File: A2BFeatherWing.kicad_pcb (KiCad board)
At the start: 2 copper layers, 50.8 x 22.9 mm, 5 parts, among them J1 Conn_01x04_Male, U1 FeatherWingTemplate, U2 AD2428W

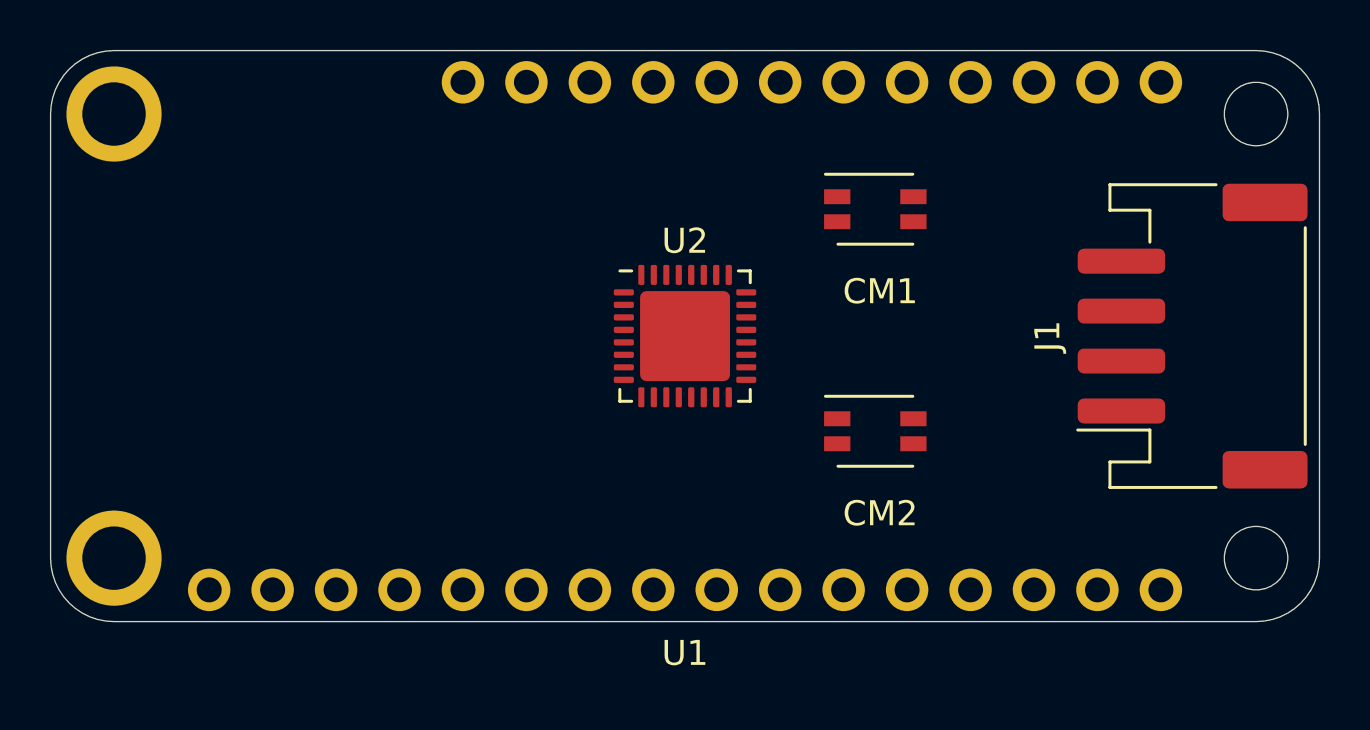
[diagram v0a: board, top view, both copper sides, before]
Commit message: added 3d model of JST PH and CM added eco layer for silkscreen
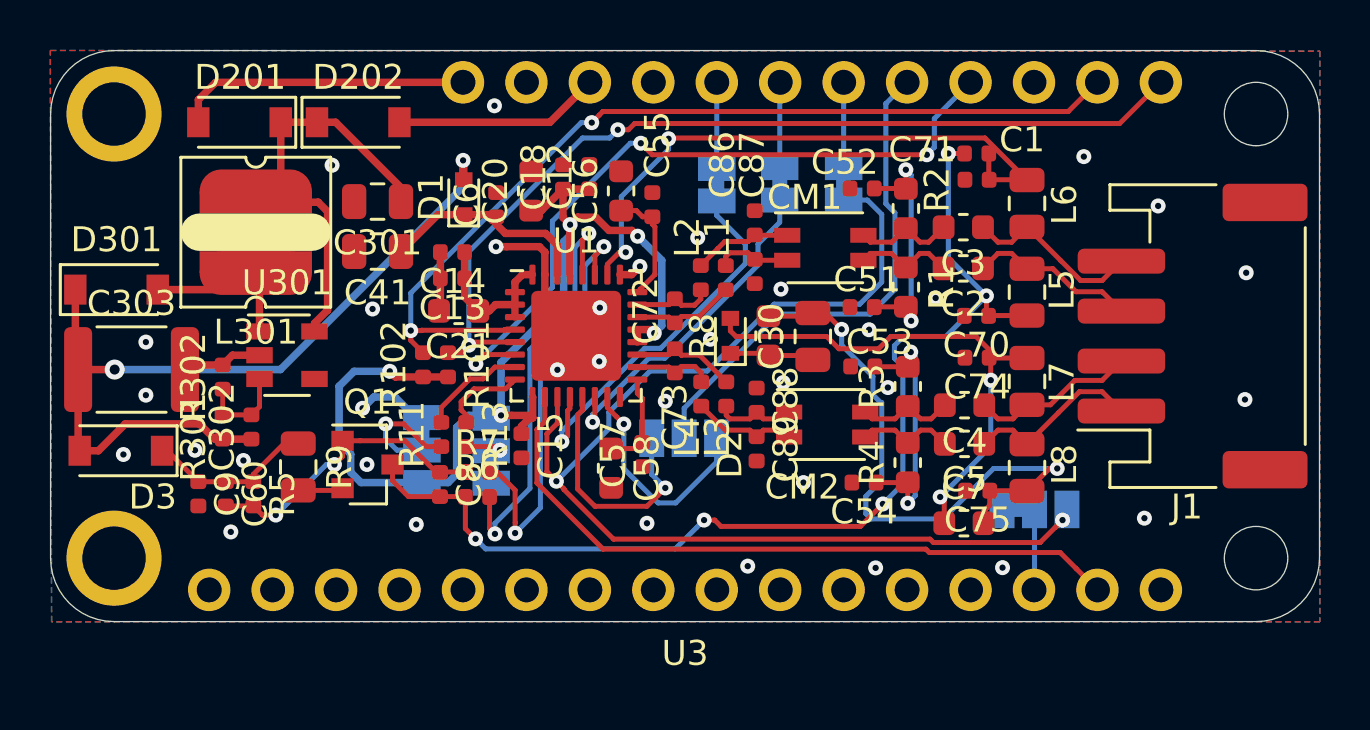
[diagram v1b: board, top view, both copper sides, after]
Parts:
- removed the CM1 at (100.3, 106.7)
- removed U2: AD2428W, Package_DFN_QFN:QFN-32-1EP_5x5mm_P0.5mm_EP3.6x3.6mm
- added C1: 33n, Capacitor_SMD:C_0402_1005Metric, F.Cu at (104.4, 104.5)
- added C12: 0u1, Capacitor_SMD:C_0402_1005Metric, F.Cu at (88.9, 105.4)
- added C13: 4n7, Capacitor_SMD:C_0402_1005Metric, F.Cu at (83.4, 109.5)
- added C14: 0u1, Capacitor_SMD:C_0402_1005Metric, F.Cu at (83.4, 108.4)
- added C15: 0u1, Capacitor_SMD:C_0402_1005Metric, F.Cu at (86.2, 116.2)
- added C18: 4n7, Capacitor_SMD:C_0402_1005Metric, F.Cu at (87.8, 105.4)
- added C2: 10n, Capacitor_SMD:C_0603_1608Metric, F.Cu at (103.8, 109.0)
- added C20: 4u7, Capacitor_SMD:C_0603_1608Metric, F.Cu at (86.5, 106.0)
- added C21: 4u7, Capacitor_SMD:C_0603_1608Metric, F.Cu at (83.7, 110.8)
- added C3: 10n, Capacitor_SMD:C_0603_1608Metric, F.Cu at (103.8, 107.4)
- added C30: 4u7, Capacitor_SMD:C_0805_2012Metric, F.Cu at (97.8, 111.8)
- added C301: 2u2, Capacitor_SMD:C_0805_2012Metric, F.Cu at (80.4, 106.4)
- added C302: 47p, Capacitor_SMD:C_0402_1005Metric, F.Cu at (75.3, 115.4)
- added C303: 22u, Capacitor_SMD:C_1812_4532Metric, F.Cu at (70.5, 113.1)
- added C4: 10n, Capacitor_SMD:C_0603_1608Metric, F.Cu at (103.9, 114.5)
- added C41: 10u, Capacitor_SMD:C_0805_2012Metric, F.Cu at (80.4, 108.4)
- added C5: 10n, Capacitor_SMD:C_0603_1608Metric, F.Cu at (103.9, 116.1)
- added C51: 33n, Capacitor_SMD:C_0402_1005Metric, F.Cu at (99.8, 110.6)
- added C52: 33n, Capacitor_SMD:C_0402_1005Metric, F.Cu at (99.8, 105.8)
- added C53: 33n, Capacitor_SMD:C_0402_1005Metric, F.Cu at (99.8, 113.0)
- added C54: 33n, Capacitor_SMD:C_0402_1005Metric, F.Cu at (99.9, 117.6)
- added C55: 0u1, Capacitor_SMD:C_0402_1005Metric, F.Cu at (91.4, 106.5)
- added C56: 4u7, Capacitor_SMD:C_0603_1608Metric, F.Cu at (90.2, 106.0)
- added C57: 0u1, Capacitor_SMD:C_0402_1005Metric, F.Cu at (91.0, 116.5)
- added C58: 4u7, Capacitor_SMD:C_0603_1608Metric, F.Cu at (89.8, 117.0)
- added C6: 0u1, Capacitor_SMD:C_0402_1005Metric, F.Cu at (85.2, 106.5)
- added C60: 15n, Capacitor_SMD:C_0402_1005Metric, F.Cu at (74.3, 118.1)
- added C7: 0u47, Capacitor_SMD:C_0603_1608Metric, F.Cu at (103.9, 119.2)
- added C70: 33n, Capacitor_SMD:C_0402_1005Metric, F.Cu at (104.4, 111.0)
- added C71: 33n, Capacitor_SMD:C_0402_1005Metric, F.Cu at (104.4, 105.5)
- added C72: 12p, Capacitor_SMD:C_0402_1005Metric, F.Cu at (92.3, 110.8)
- added C73: 12p, Capacitor_SMD:C_0402_1005Metric, F.Cu at (92.3, 112.8)
- added C74: 33n, Capacitor_SMD:C_0402_1005Metric, F.Cu at (104.4, 112.6)
- added C75: 33n, Capacitor_SMD:C_0402_1005Metric, F.Cu at (104.4, 118.0)
- added C8: 3n3, Capacitor_SMD:C_0402_1005Metric, F.Cu at (82.9, 117.7)
- added C86: 27p, Capacitor_SMD:C_0402_1005Metric, F.Cu at (95.5, 109.2)
- added C87: 27p, Capacitor_SMD:C_0402_1005Metric, F.Cu at (95.5, 107.2)
- added C88: 27p, Capacitor_SMD:C_0402_1005Metric, F.Cu at (95.6, 114.3)
- added C89: 27p, Capacitor_SMD:C_0402_1005Metric, F.Cu at (95.6, 116.3)
- added C9: 33n, Capacitor_SMD:C_0402_1005Metric, F.Cu at (73.2, 118.1)
- added CM2: ACT1210-510-2P-TL00, A2BFeatherWing:CommonModeChoke_TDK_ACT1210, F.Cu at (98.4, 115.3)
- added D1: RB521S30, Diode_SMD:D_SOD-523, F.Cu at (83.8, 106.2)
- added D2: RB521S30, Diode_SMD:D_SOD-523, F.Cu at (94.5, 111.8)
- added D201: MBR0520, Diode_SMD:D_SOD-123, F.Cu at (74.9, 103.2)
- added D202: MBR0520, Diode_SMD:D_SOD-123, F.Cu at (79.6, 103.2)
- added D3: SS16HE3_B/H, Diode_SMD:D_SOD-123, F.Cu at (70.1, 116.3)
- added D301: MBR0520, Diode_SMD:D_SOD-123, F.Cu at (70.0, 109.9)
- added JP1: SolderJumper_3_Bridged12, Jumper:SolderJumper-3_P1.3mm_Bridged12_Pad1.0x1.5mm, B.Cu at (82.2, 116.3)
- added JP101: MCLK_D0_WS, Jumper:SolderJumper-3_P1.3mm_Bridged12_Pad1.0x1.5mm, B.Cu at (106.7, 118.7)
- added JP102: SD_D11, Jumper:SolderJumper-2_P1.3mm_Bridged_Pad1.0x1.5mm, B.Cu at (96.5, 105.7)
- added JP103: SDI_D12, Jumper:SolderJumper-2_P1.3mm_Bridged_Pad1.0x1.5mm, B.Cu at (94.0, 105.7)
- added JP104: WS_D10, Jumper:SolderJumper-2_P1.3mm_Bridged_Pad1.0x1.5mm, B.Cu at (99.1, 105.7)
- added JP105: SDO1_D9_SDI1, Jumper:SolderJumper-3_P1.3mm_Open_Pad1.0x1.5mm, B.Cu at (92.7, 115.8)
- added JP2: SolderJumper_3_Bridged12, Jumper:SolderJumper-3_P1.3mm_Bridged12_Pad1.0x1.5mm, B.Cu at (85.0, 116.3)
- added L1: 180n, Inductor_SMD:L_0402_1005Metric, F.Cu at (94.3, 109.4)
- added L2: 180n, Inductor_SMD:L_0402_1005Metric, F.Cu at (93.3, 109.4)
- added L3: 180n, Inductor_SMD:L_0402_1005Metric, F.Cu at (94.4, 114.1)
- added L301: 4.7uH, A2BFeatherWing:L_Sumida_CR43_4.3x4.8x3.5mm, F.Cu at (75.5, 107.6)
- added L4: 180n, Inductor_SMD:L_0402_1005Metric, F.Cu at (93.4, 114.1)
- added L5: 3u3, Inductor_SMD:L_0805_2012Metric, F.Cu at (106.4, 110.0)
- added L6: 3u3, Inductor_SMD:L_0805_2012Metric, F.Cu at (106.4, 106.5)
- added L7: 3u3, Inductor_SMD:L_0805_2012Metric, F.Cu at (106.4, 113.6)
- added L8: 3u3, Inductor_SMD:L_0805_2012Metric, F.Cu at (106.4, 117.0)
- added Q1: Q_PMOS_GDS, Package_TO_SOT_SMD:SOT-23, F.Cu at (80.0, 116.9)
- added R1: 120, Resistor_SMD:R_0603_1608Metric, F.Cu at (101.5, 109.8)
- added R101: 2k7, Resistor_SMD:R_0402_1005Metric, F.Cu at (83.2, 112.9)
- added R102: 2k7, Resistor_SMD:R_0402_1005Metric, F.Cu at (82.2, 112.9)
- added R11: 10k, Resistor_SMD:R_0402_1005Metric, F.Cu at (83.0, 115.7)
- added R13: 10k, Resistor_SMD:R_0402_1005Metric, F.Cu at (84.0, 115.7)
- added R2: 120, Resistor_SMD:R_0603_1608Metric, F.Cu at (101.5, 106.7)
- added R3: 120, Resistor_SMD:R_0603_1608Metric, F.Cu at (101.6, 113.8)
- added R301: 60k4, Resistor_SMD:R_0402_1005Metric, F.Cu at (74.2, 115.4)
- added R302: 11k3, Resistor_SMD:R_0402_1005Metric, F.Cu at (74.2, 113.4)
- added R4: 120, Resistor_SMD:R_0603_1608Metric, F.Cu at (101.6, 116.8)
- added R5: 33k, Resistor_SMD:R_0402_1005Metric, F.Cu at (75.4, 118.1)
- added R6: 1k, Resistor_SMD:R_0402_1005Metric, F.Cu at (84.4, 118.2)
- added R7: 3k3, Resistor_SMD:R_0402_1005Metric, F.Cu at (84.4, 117.2)
- added R8: 4k7, Resistor_SMD:R_0603_1608Metric, F.Cu at (96.0, 111.8)
- added R9: 1r, Resistor_SMD:R_0805_2012Metric, F.Cu at (77.2, 117.0)
- added U3: FeatherWingTemplate, Knochi_Modules:FeatherWingTemplate, F.Cu at (92.7, 111.8)
- added U301: LT1930A, Package_TO_SOT_SMD:SOT-23-5, F.Cu at (76.8, 112.5)
- CM1: renamed from CM2; footprint Knochi_Filters:CommonModeChoke_TDK_ACT1210 -> A2BFeatherWing:CommonModeChoke_TDK_ACT1210
- U1: value FeatherWingTemplate -> AD2428W; footprint Knochi_Modules:FeatherWingTemplate -> Package_DFN_QFN:QFN-32-1EP_5x5mm_P0.5mm_EP3.6x3.6mm
- moved CM1 7.61 mm to (98.3, 108.2)
- moved U1 4.36 mm to (88.3, 111.8)
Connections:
- net Net-(U1-Pad16) renamed /A2B/IO7
- CM1 pad 1: Net-(CM2-Pad1) -> /A2B/B''N
- CM1 pad 2: Net-(CM2-Pad2) -> /A2B/B'N
- CM1 pad 3: Net-(CM2-Pad3) -> /A2B/B''P
- CM1 pad 4: Net-(CM2-Pad4) -> /A2B/B'P
- J1 pad 1: Net-(J1-Pad1) -> /A2B/AN
- J1 pad 2: Net-(J1-Pad2) -> /A2B/AP
- J1 pad 3: Net-(J1-Pad3) -> /A2B/BP
- J1 pad 4: Net-(J1-Pad4) -> /A2B/BN
- U1 pad 1: Net-(U1-Pad1) -> +1V9
- U1 pad 10: Net-(U1-Pad10) -> /BCLK
- U1 pad 11: Net-(U1-Pad11) -> /SYNC
- U1 pad 12: Net-(U1-Pad12) -> /SDI_0
- U1 pad 13: Net-(U1-Pad13) -> /SDI_1
- U1 pad 14: Net-(U1-Pad14) -> /SDO_0
- U1 pad 15: Net-(U1-Pad15) -> /SDO_1
- U1 pad 18: Net-(U1-Pad18) -> /A2B/A'''N
- U1 pad 19: Net-(U1-Pad19) -> /A2B/A'''P
- U1 pad 2: Net-(U1-Pad2) -> +1V9
- U1 pad 20: Net-(U1-Pad20) -> +3V3
- U1 pad 21: Net-(U1-Pad21) -> +3V3
- U1 pad 22: Net-(U1-Pad22) -> /A2B/B'''P
- U1 pad 23: Net-(U1-Pad23) -> /A2B/B'''N
- U1 pad 25: Net-(U1-Pad25) -> GND
- U1 pad 3: Net-(U1-Pad3) -> +1V9
- U1 pad 4: Net-(U1-Pad4) -> /SCL
- U1 pad 5: Net-(U1-Pad5) -> /SDA
- U1 pad 6: Net-(U1-Pad6) -> /IRQ
- U1 pad 7: Net-(U1-Pad7) -> /A2B/IO1
- U1 pad 8: Net-(U1-Pad8) -> /A2B/IO2
- U1 pad 9: Net-(U1-Pad9) -> +3V3
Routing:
- net /SYNC: track 0.00 -> 46.6 mm, vias 0 -> 2
- net Net-(C1-Pad1): track 0.00 -> 43.9 mm, vias 0 -> 5
- net +3V3: track 0.00 -> 43.6 mm, vias 0 -> 5
- net /SCL: track 0.00 -> 37.8 mm, vias 0 -> 2
- net /SDA: track 0.00 -> 37.1 mm, vias 0 -> 2
- net +9V: track 0.00 -> 34.4 mm, vias 0 -> 2
- net /IRQ: track 0.00 -> 28.8 mm, vias 0 -> 3
- net /BCLK: track 0.00 -> 27.8 mm
- net Net-(C30-Pad2): track 0.00 -> 24.7 mm, vias 0 -> 2
- net Net-(C1-Pad2): track 0.00 -> 24.4 mm, vias 0 -> 2
- net Net-(C7-Pad1): track 0.00 -> 20.9 mm, vias 0 -> 2
- net /SD1: track 0.00 -> 20.4 mm
- net +4V: track 0.00 -> 18.1 mm
- net Net-(R7-Pad2): track 0.00 -> 17.2 mm, vias 0 -> 2
- net Net-(R6-Pad2): track 0.00 -> 16.9 mm, vias 0 -> 2
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- added copper zone on B.Cu, net GND
- added copper zone on F.Cu, net GND
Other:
- net class Default: trace_width 0.25 -> 0.2; via_dia 0.8 -> 0.6; via_drill 0.4 -> 0.25
- net class Power added: clearance 0.2, trace_width 0.3, via_dia 0.6, via_drill 0.25
- rule via_min_drill: 0.3 -> 0.25
- rule via_min_size: 0.4 -> 0.6
- board text added: "0"
- board text added: "13"
- board text added: "3V"
- board text added: "5"
- board text added: "A0"
- board text added: "A1"
- board text added: "A2"
- board text added: "A3"
- board text added: "A4"
- board text added: "A5"
- board text added: "ARf"
- board text added: "BAT"
- board text added: "BCLK"
- board text added: "En"
- board text added: "GND"
- board text added: "IRQ"
- board text added: "MCLK"
- board text added: "RST"
- board text added: "SCL"
- board text added: "SD1"
- board text added: "SDA"
- board text added: "SDI"
- board text added: "SDO"
- board text added: "SPI"
- board text added: "USB"
- board text added: "WS"

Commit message: - added documentation - removed MCLK
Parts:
- JP101: value MCLK_D0_WS -> WS_D0; footprint Jumper:SolderJumper-3_P1.3mm_Bridged12_Pad1.0x1.5mm -> Jumper:SolderJumper-2_P1.3mm_Open_Pad1.0x1.5mm
- moved JP101 0.62 mm to (107.3, 118.6), turned to 180 degrees
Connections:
- JP101 pad 1: /MCLK -> /SYNC
